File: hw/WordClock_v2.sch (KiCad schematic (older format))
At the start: 22 parts, among them M1 ESP-07, P1 5V_input, P2 WS2812b_Out, P3 UART, SW1 DPST, U1 NCP1117ST33T3G, U2 DS3232, U4 WS2812b

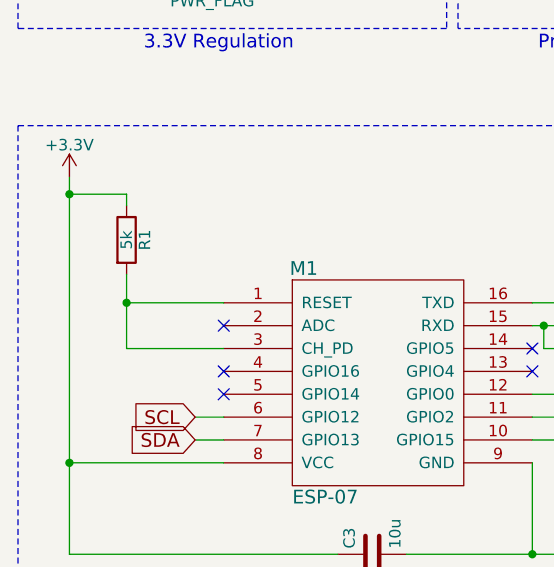
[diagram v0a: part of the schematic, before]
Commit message: Updated CH_PD and RST on ESP to use their own pullup resistors. Attached GPIO16 to RST to allow wake from deep sleep
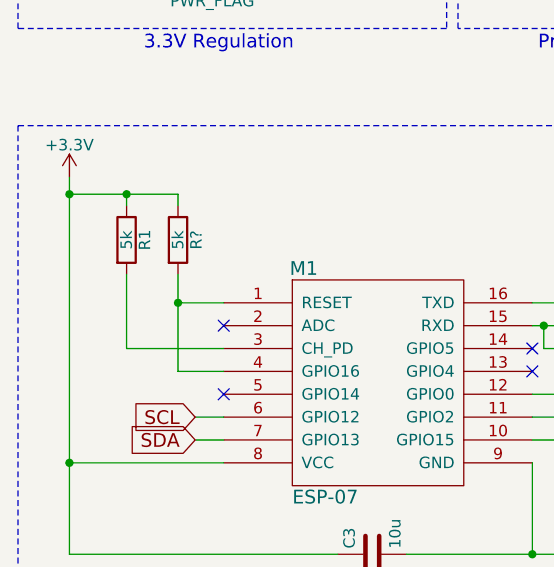
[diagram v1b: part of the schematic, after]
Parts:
- added R?: 5k, FabLibrary:C_1206_HandSoldering_IainEdit, symbol R
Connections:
- net +3V3: now also R?.1
- net at M1.3 (CH_PD), R1.2: no longer M1.1 (RESET)
- net at M1.4 (GPIO16): now also M1.1 (RESET), R?.2
- no-connect marks 11 -> 10
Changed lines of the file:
@@
 LIBS:contrib
 LIBS:valves
-LIBS:IainPersonalLibrary
 LIBS:WordClock_v2-cache
 EELAYER 25 0
@@
 	2750 3700 2850 3700
 Wire Wire Line
-	725  2825 975  2825
+	725  2825 1200 2825
 Wire Wire Line
 	975  2825 975  2875
 Connection ~ 725  2825
-Wire Wire Line
-	975  3500 1400 3500
-Wire Wire Line
-	975  3175 975  3500
-Wire Wire Line
-	1400 3300 975  3300
-Connection ~ 975  3300
 Wire Notes Line
 	2425 2100 2425 600
@@
 	1    0    0    -1
 $EndComp
-NoConn ~ 1400 3600
 Wire Wire Line
 	5700 3200 5475 3200
@@
 $EndComp
 Connection ~ 6325 1150
+$Comp
+L R R?
+U 1 1 595AA86F
+P 1200 3025
+F 0 "R?" V 1280 3025 50  0000 C CNN
+F 1 "5k" V 1200 3025 50  0000 C CNN
+F 2 "FabLibrary:C_1206_HandSoldering_IainEdit" V 1130 3025 30  0001 C CNN
+F 3 "" H 1200 3025 30  0000 C CNN
+	1    1200 3025
+	1    0    0    -1
+$EndComp
+Wire Wire Line
+	1200 2825 1200 2875
+Connection ~ 975  2825
+Wire Wire Line
+	1200 3175 1200 3600
+Wire Wire Line
+	1200 3300 1400 3300
+Wire Wire Line
+	1400 3500 975  3500
+Wire Wire Line
+	975  3500 975  3175
+Wire Wire Line
+	1200 3600 1400 3600
+Connection ~ 1200 3300
 $EndSCHEMATC
